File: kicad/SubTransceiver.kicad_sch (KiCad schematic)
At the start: 58 parts

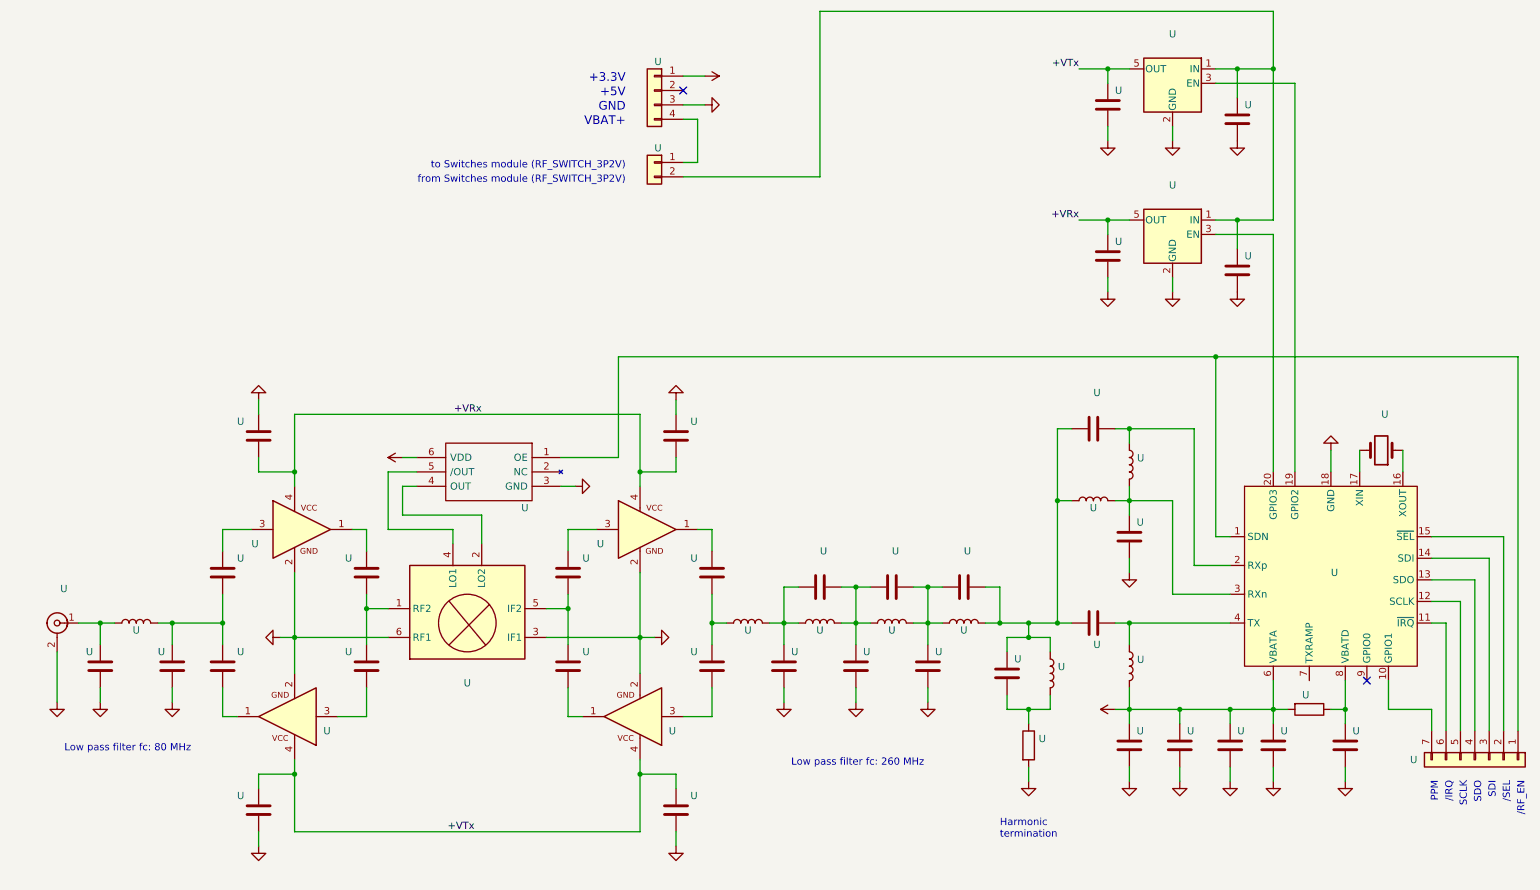
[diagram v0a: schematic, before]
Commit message: Adding PIB USB BRIDGE UML state diagrams - WIP
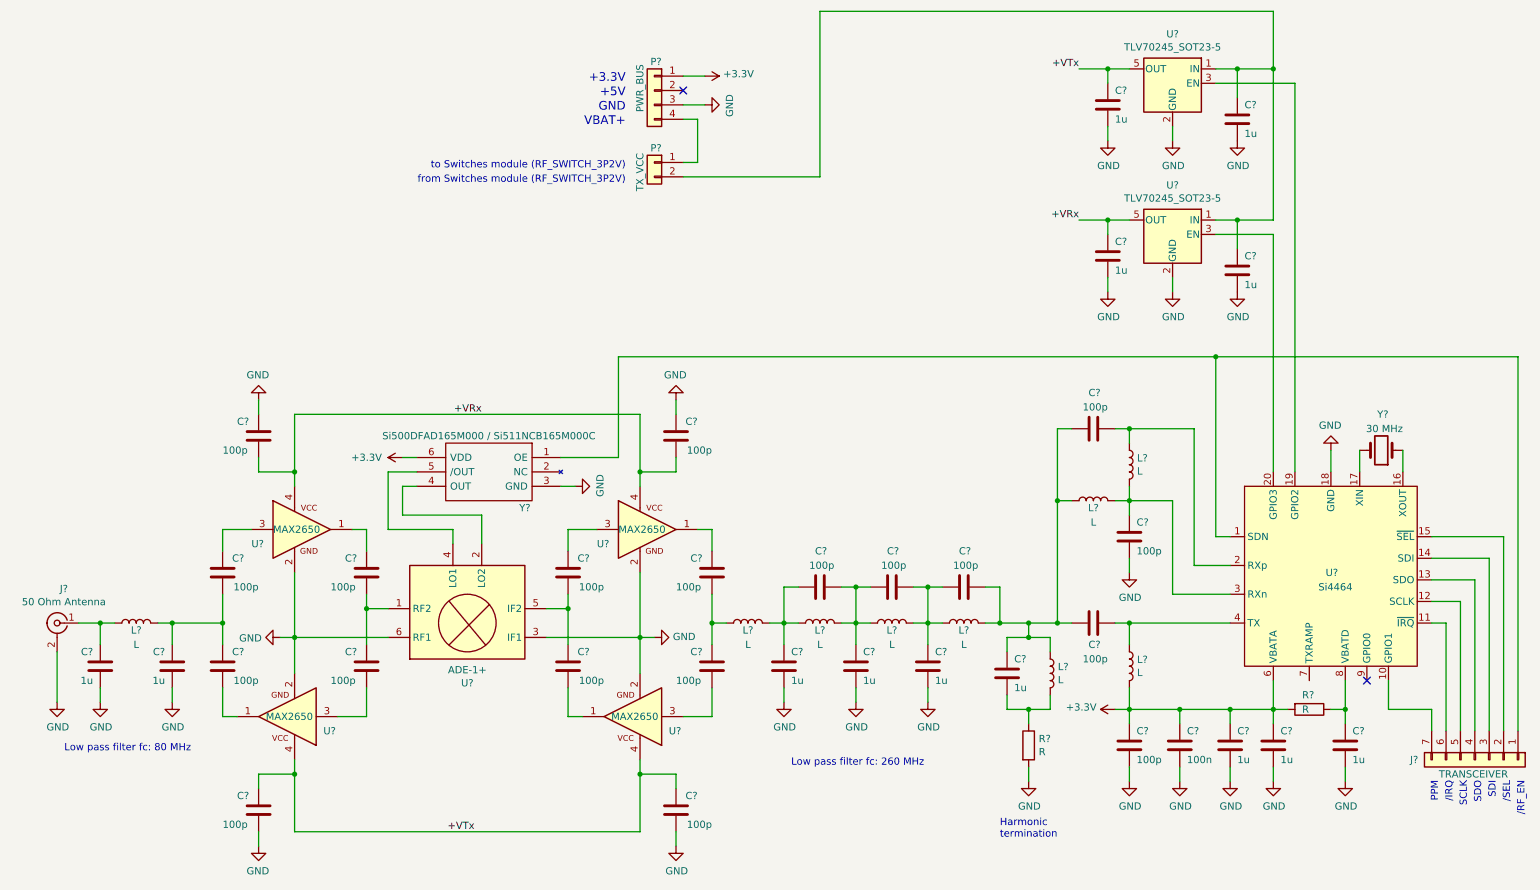
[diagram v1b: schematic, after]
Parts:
- C? (x13): renamed from U; value (none) -> 1u; symbol device:C -> RCTX-rescue:C-device
- C? (x19): renamed from U; value (none) -> 100p; symbol device:C -> RCTX-rescue:C-device
- C?: renamed from U; value (none) -> 100n; symbol device:C -> RCTX-rescue:C-device
- J?: renamed from U; value (none) -> 50 Ohm Antenna; symbol conn:Conn_Coaxial -> RCTX-rescue:Conn_Coaxial-conn
- J?: renamed from U; value (none) -> TRANSCEIVER; symbol conn:Conn_01x07 -> RCTX-rescue:Conn_01x07-conn
- L? (x9): renamed from U; value (none) -> L; symbol device:L -> RCTX-rescue:L-device
- P?: renamed from U; value (none) -> TX_VCC; footprint (none) -> Connectors_Samtec:SL-102-X-XX_1x02
- P?: renamed from U; value (none) -> PWR_BUS; footprint (none) -> Connectors_Samtec:SL-104-X-XX_1x04
- R? (x2): renamed from U; value (none) -> R; symbol device:R -> RCTX-rescue:R-device
- U?: renamed from U; value (none) -> Si4464; footprint (none) -> Package_DFN_QFN:QFN-20-1EP_4x4mm_P0.5mm_EP2.6x2.6mm_ThermalVias; symbol RF:Si4464 -> RCTX-rescue:Si4464-RF
- U? (x2): renamed from U; value (none) -> TLV70245_SOT23-5; footprint (none) -> TO_SOT_Packages_SMD:SOT-23-5; symbol regul:TLV70245_SOT23-5 -> RCTX-rescue:TLV70245_SOT23-5-regul
- U? (x4): renamed from U; value (none) -> MAX2650; footprint (none) -> smd-semi:SOT-143; symbol maxim_1:MAX2650 -> RCTX-rescue:MAX2650-maxim_1
- U?: renamed from U; value (none) -> ADE-1+; footprint (none) -> RF_Mini-Circuits:Mini-Circuits_CD542_LandPatternPL-052; symbol RF_Mixer:ADE-1+ -> RCTX-rescue:ADE-1+-RF_Mixer
- Y?: renamed from U; value (none) -> 30 MHz; symbol device:Crystal -> RCTX-rescue:Crystal-device
- Y?: renamed from U; value (none) -> Si500DFAD165M000 / Si511NCB165M000C; footprint (none) -> Si500D; symbol Si500D:Si500D -> RCTX-rescue:Si500D-Si500D
